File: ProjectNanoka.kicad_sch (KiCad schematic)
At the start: 32 parts, among them K1 2-1462038-1, P1 ST_20A, Q1 2N3904BU, Q2 2N3904BU, U1 TLV70033DDCR, U2 NC7WZ16P6X, U3 PS1440P02BT

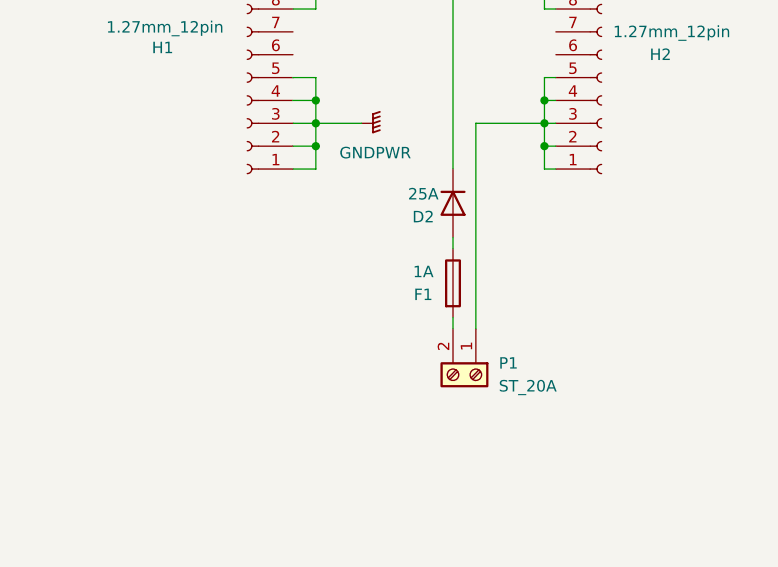
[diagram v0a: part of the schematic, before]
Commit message: Modified decoupling problem at layout
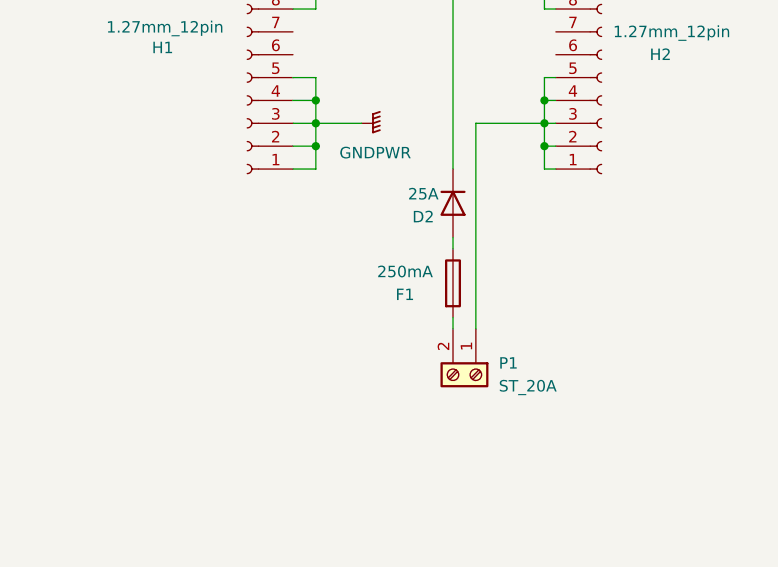
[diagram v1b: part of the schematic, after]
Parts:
- F1: value 1A -> 250mA
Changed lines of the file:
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@@
 		(dnp no)
 		(property "Reference" "F1"
-			(at 249.428 153.67 0)
+			(at 247.396 153.67 0)
 			(effects
 				(font
@@
 			)
 		)
-		(property "Value" "1A"
-			(at 249.428 151.13 0)
+		(property "Value" "250mA"
+			(at 247.396 151.13 0)
 			(effects
 				(font
